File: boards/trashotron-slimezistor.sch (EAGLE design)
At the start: 10 parts, among them U1 LM358

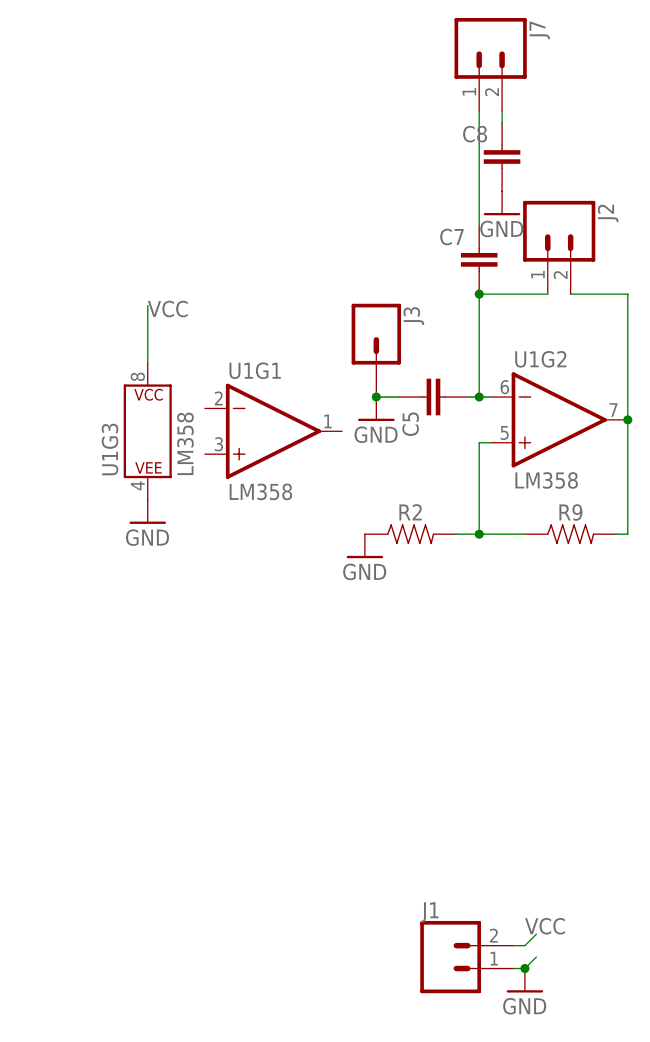
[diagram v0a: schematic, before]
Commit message: this version of the boards is now all tested out on solderless breadboard
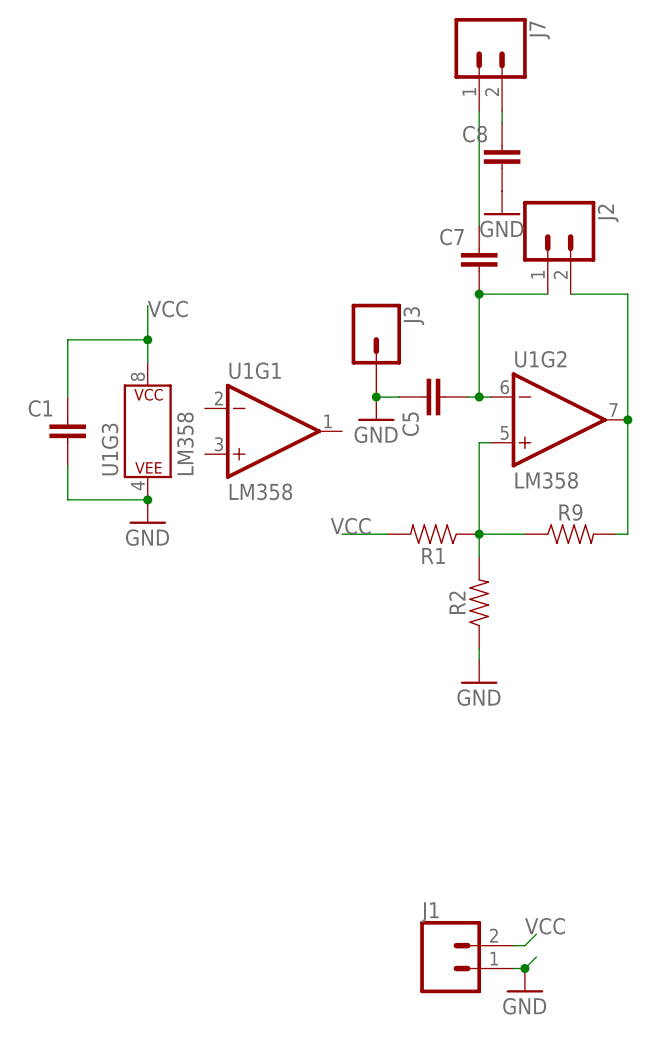
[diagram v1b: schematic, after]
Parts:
- added C1: (no value), rcl:C-EU050-050X075
- added R1: (no value), SparkFun-Resistors:RESISTORAXIAL-0.3
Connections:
- net GND: now also C1.2
- net N$10: now also R1.1
- net VCC: now also C1.1, R1.2
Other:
- moved on the sheet: R2
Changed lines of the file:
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@@
 <part name="J2" library="SparkFun-Connectors" deviceset="CONN_02" device=""/>
 <part name="J3" library="SparkFun-Connectors" deviceset="CONN_01" device=""/>
+<part name="C1" library="rcl" library_urn="urn:adsk.eagle:library:334" deviceset="C-EU" device="050-050X075" package3d_urn="urn:adsk.eagle:package:23665/1"/>
+<part name="R1" library="SparkFun-Resistors" deviceset="RESISTOR" device="AXIAL-0.3" value=" "/>
 </parts>
 <sheets>
@@
 <attribute name="VALUE" x="33.02" y="82.55" size="1.778" layer="95" font="vector" rot="R90"/>
 </instance>
-<instance part="R2" gate="G$1" x="57.15" y="76.2" smashed="yes">
-<attribute name="NAME" x="57.15" y="77.724" size="1.778" layer="95" font="vector" align="bottom-center"/>
-<attribute name="VALUE" x="57.15" y="74.676" size="1.778" layer="96" font="vector" align="top-center"/>
+<instance part="R2" gate="G$1" x="64.77" y="68.58" smashed="yes" rot="R90">
+<attribute name="NAME" x="63.246" y="68.58" size="1.778" layer="95" font="vector" rot="R90" align="bottom-center"/>
+<attribute name="VALUE" x="66.294" y="68.58" size="1.778" layer="96" font="vector" rot="R90" align="top-center"/>
 </instance>
 <instance part="C7" gate="G$1" x="64.77" y="107.95" smashed="yes" rot="MR0">
@@
 <attribute name="VALUE" x="74.93" y="74.676" size="1.778" layer="96" font="vector" align="top-center"/>
 </instance>
-<instance part="GND17" gate="1" x="52.07" y="73.66" smashed="yes">
-<attribute name="VALUE" x="49.53" y="71.12" size="1.778" layer="96"/>
+<instance part="GND17" gate="1" x="64.77" y="59.69" smashed="yes">
+<attribute name="VALUE" x="62.23" y="57.15" size="1.778" layer="96"/>
 </instance>
 <instance part="GND18" gate="1" x="67.31" y="111.76" smashed="yes">
@@
 <attribute name="VALUE" x="48.514" y="101.6" size="1.778" layer="96" font="vector" rot="R270"/>
 <attribute name="NAME" x="56.388" y="101.6" size="1.778" layer="95" font="vector" rot="R270"/>
+</instance>
+<instance part="C1" gate="G$1" x="19.05" y="88.9" smashed="yes" rot="MR0">
+<attribute name="NAME" x="17.526" y="89.281" size="1.778" layer="95" rot="MR0"/>
+<attribute name="VALUE" x="17.526" y="84.201" size="1.778" layer="96" rot="MR0"/>
+</instance>
+<instance part="R1" gate="G$1" x="59.69" y="76.2" smashed="yes" rot="R180">
+<attribute name="NAME" x="59.69" y="74.676" size="1.778" layer="95" font="vector" rot="R180" align="bottom-center"/>
+<attribute name="VALUE" x="59.69" y="77.724" size="1.778" layer="96" font="vector" rot="R180" align="top-center"/>
 </instance>
 </instances>
@@
 <pinref part="U1" gate="G3" pin="P$V-"/>
 <pinref part="GND3" gate="1" pin="GND"/>
+<pinref part="C1" gate="G$1" pin="2"/>
+<wire x1="27.94" y1="80.01" x2="19.05" y2="80.01" width="0.1524" layer="91"/>
+<wire x1="19.05" y1="80.01" x2="19.05" y2="83.82" width="0.1524" layer="91"/>
+<junction x="27.94" y="80.01"/>
 </segment>
 <segment>
@@
 <pinref part="R2" gate="G$1" pin="1"/>
 <pinref part="GND17" gate="1" pin="GND"/>
+<wire x1="64.77" y1="63.5" x2="64.77" y2="62.23" width="0.1524" layer="91"/>
 </segment>
 <segment>
@@
 <segment>
 <pinref part="U1" gate="G3" pin="P$V+"/>
-<wire x1="27.94" y1="95.25" x2="27.94" y2="101.6" width="0.1524" layer="91"/>
+<wire x1="27.94" y1="95.25" x2="27.94" y2="97.79" width="0.1524" layer="91"/>
 <label x="27.94" y="100.33" size="1.778" layer="95"/>
+<pinref part="C1" gate="G$1" pin="1"/>
+<wire x1="27.94" y1="97.79" x2="27.94" y2="101.6" width="0.1524" layer="91"/>
+<wire x1="19.05" y1="91.44" x2="19.05" y2="97.79" width="0.1524" layer="91"/>
+<wire x1="19.05" y1="97.79" x2="27.94" y2="97.79" width="0.1524" layer="91"/>
+<junction x="27.94" y="97.79"/>
+</segment>
+<segment>
+<pinref part="R1" gate="G$1" pin="2"/>
+<wire x1="54.61" y1="76.2" x2="49.53" y2="76.2" width="0.1524" layer="91"/>
+<label x="48.26" y="76.2" size="1.778" layer="95"/>
 </segment>
 </net>
@@
 <wire x1="69.85" y1="76.2" x2="64.77" y2="76.2" width="0.1524" layer="91"/>
 <pinref part="U1" gate="G2" pin="+IN"/>
-<wire x1="64.77" y1="76.2" x2="62.23" y2="76.2" width="0.1524" layer="91"/>
+<wire x1="64.77" y1="76.2" x2="64.77" y2="73.66" width="0.1524" layer="91"/>
 <wire x1="66.04" y1="86.36" x2="64.77" y2="86.36" width="0.1524" layer="91"/>
 <wire x1="64.77" y1="86.36" x2="64.77" y2="76.2" width="0.1524" layer="91"/>
 <junction x="64.77" y="76.2"/>
+<pinref part="R1" gate="G$1" pin="1"/>
 </segment>
 </net>
